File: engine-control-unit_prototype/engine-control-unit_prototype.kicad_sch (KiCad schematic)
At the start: 164 parts, among them J1 PORT_G, J2 PORT_E, J3 PORT_F, J4 PORT_A, J5 PORT_B, J6 PORT_D, J7 PORT_C, SW1 BOOT, U1 STM32H747II, Y1 32.768KHz, Y2 25MHz

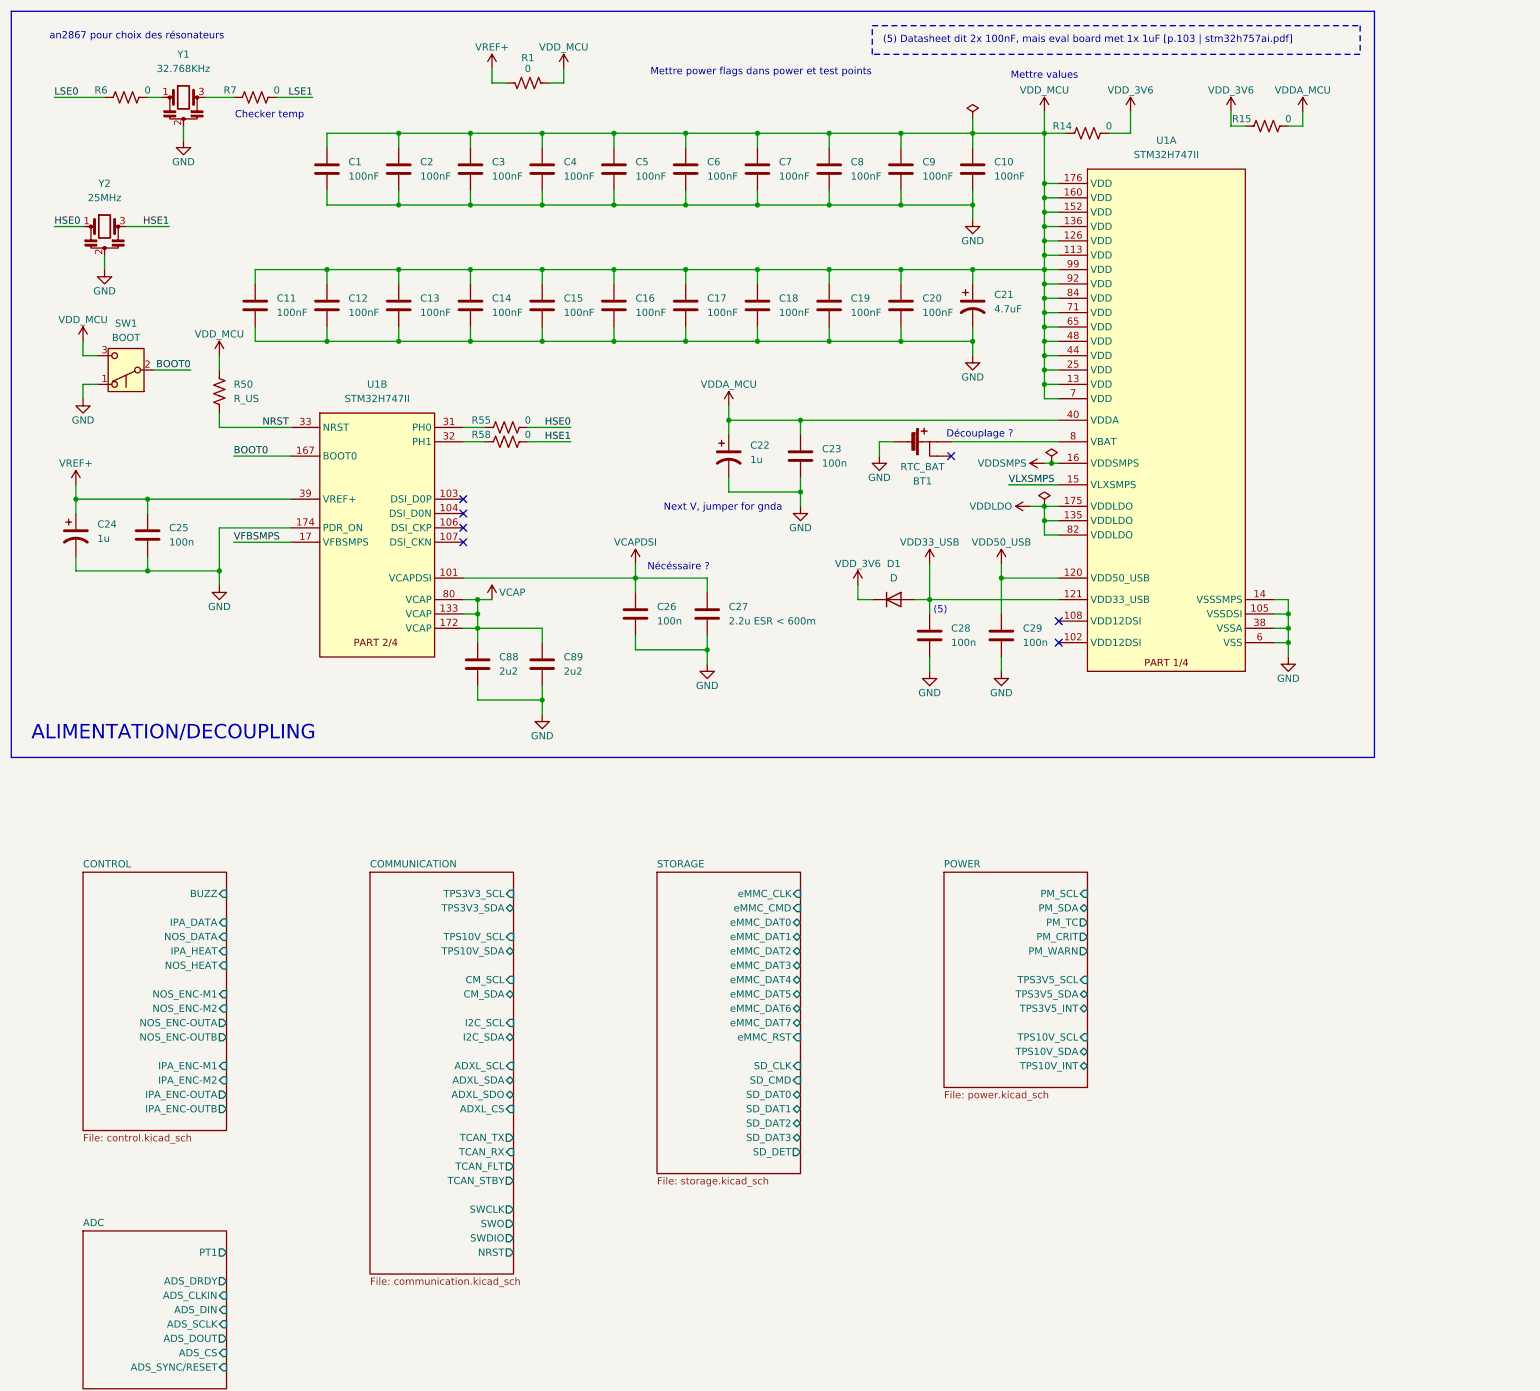
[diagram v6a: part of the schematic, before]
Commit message: Started layout Added some footprints
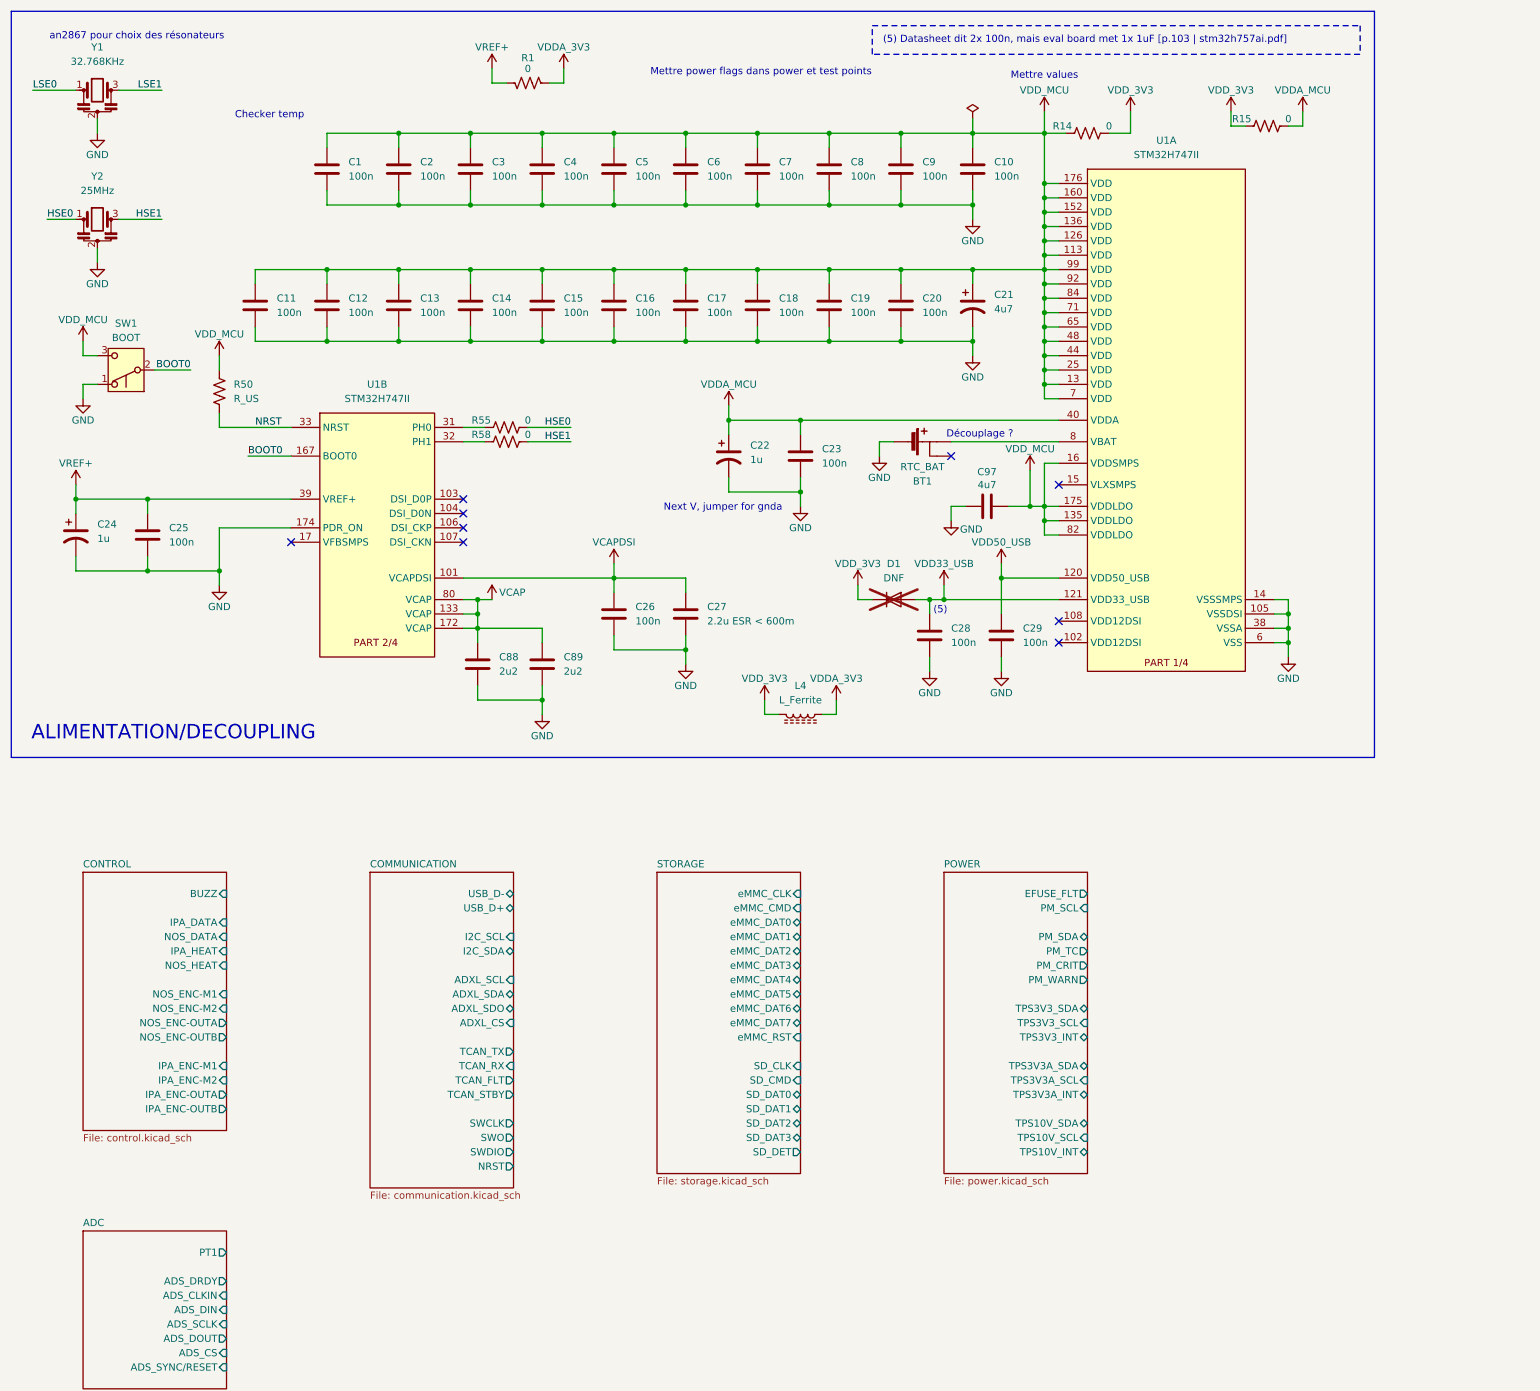
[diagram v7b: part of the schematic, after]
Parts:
- removed R6, R7: 0, Resistor_SMD:R_0201_0603Metric, symbol Device:R_US
- added C97: 4u7, Capacitor_SMD:C_0603_1608Metric, symbol Device:C
- added L4: L_Ferrite, Inductor_SMD:L_0603_1608Metric, symbol Device:L_Ferrite
- C1, C10, C11, C12, C13, C14, C15, C16, C17, C18, C19, C2, C20, C3, C4, C5, C6, C7, C8, C9: value 100nF -> 100n; footprint Capacitor_SMD:C_0603_1608Metric -> Capacitor_SMD:C_0402_1005Metric
- C21: value 4.7uF -> 4u7
- C23, C25, C26, C28, C29: footprint Capacitor_SMD:C_0603_1608Metric -> Capacitor_SMD:C_0402_1005Metric
- C27: footprint (none) -> Capacitor_SMD:C_0603_1608Metric
- D1: value D -> DNF; now not fitted
- J1, J2, J3, J4, J5, J6, J7: footprint (none) -> Connector_PinSocket_2.54mm:PinSocket_1x16_P2.54mm_Vertical
- SW1: footprint (none) -> Connector_PinSocket_2.54mm:PinSocket_1x03_P2.54mm_Vertical
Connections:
- net VDDLDO is gone; now on net VDD_MCU: U1.135 (VDDLDO), U1.175 (VDDLDO), U1.82 (VDDLDO)
- net VDDSMPS is gone; now on net VDD_MCU: U1.16 (VDDSMPS)
- net GND: now also C97.1
- net LSE0: now also Y1.1
- net LSE1: now also Y1.3
- net VDD_MCU: now also C97.2; no longer R1.1
- net VDD_3V6 renamed VDD_3V3
- net VDD_3V3: now also L4.2
- net VFBSMPS: no longer names the net of U1.17 (VFBSMPS)
- net VLXSMPS: no longer names the net of U1.15 (VLXSMPS)
- new net VDDA_3V3: L4.1, R1.1
- no-connect marks 7 -> 9
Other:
- sheet COMMUNICATION ports: added USB_D+, USB_D-; removed CM_SCL, CM_SDA, TPS10V_SCL, TPS10V_SDA, TPS3V3_SCL, TPS3V3_SDA
- sheet POWER ports: added EFUSE_FLT, TPS3V3A_INT, TPS3V3A_SCL, TPS3V3A_SDA, TPS3V3_INT, TPS3V3_SCL, TPS3V3_SDA; removed TPS3V5_INT, TPS3V5_SCL, TPS3V5_SDA
- note added: "(5) Datasheet dit 2x 100n, mais eval board met 1x 1uF [p.103 | stm32h757ai.pdf]"
- note removed: "(5) Datasheet dit 2x 100nF, mais eval board met 1x 1uF [p.103 | stm32h757ai.pdf]"
- note removed: "Nécéssaire ?"
- moved on the sheet: C26, C27, Y1, Y2

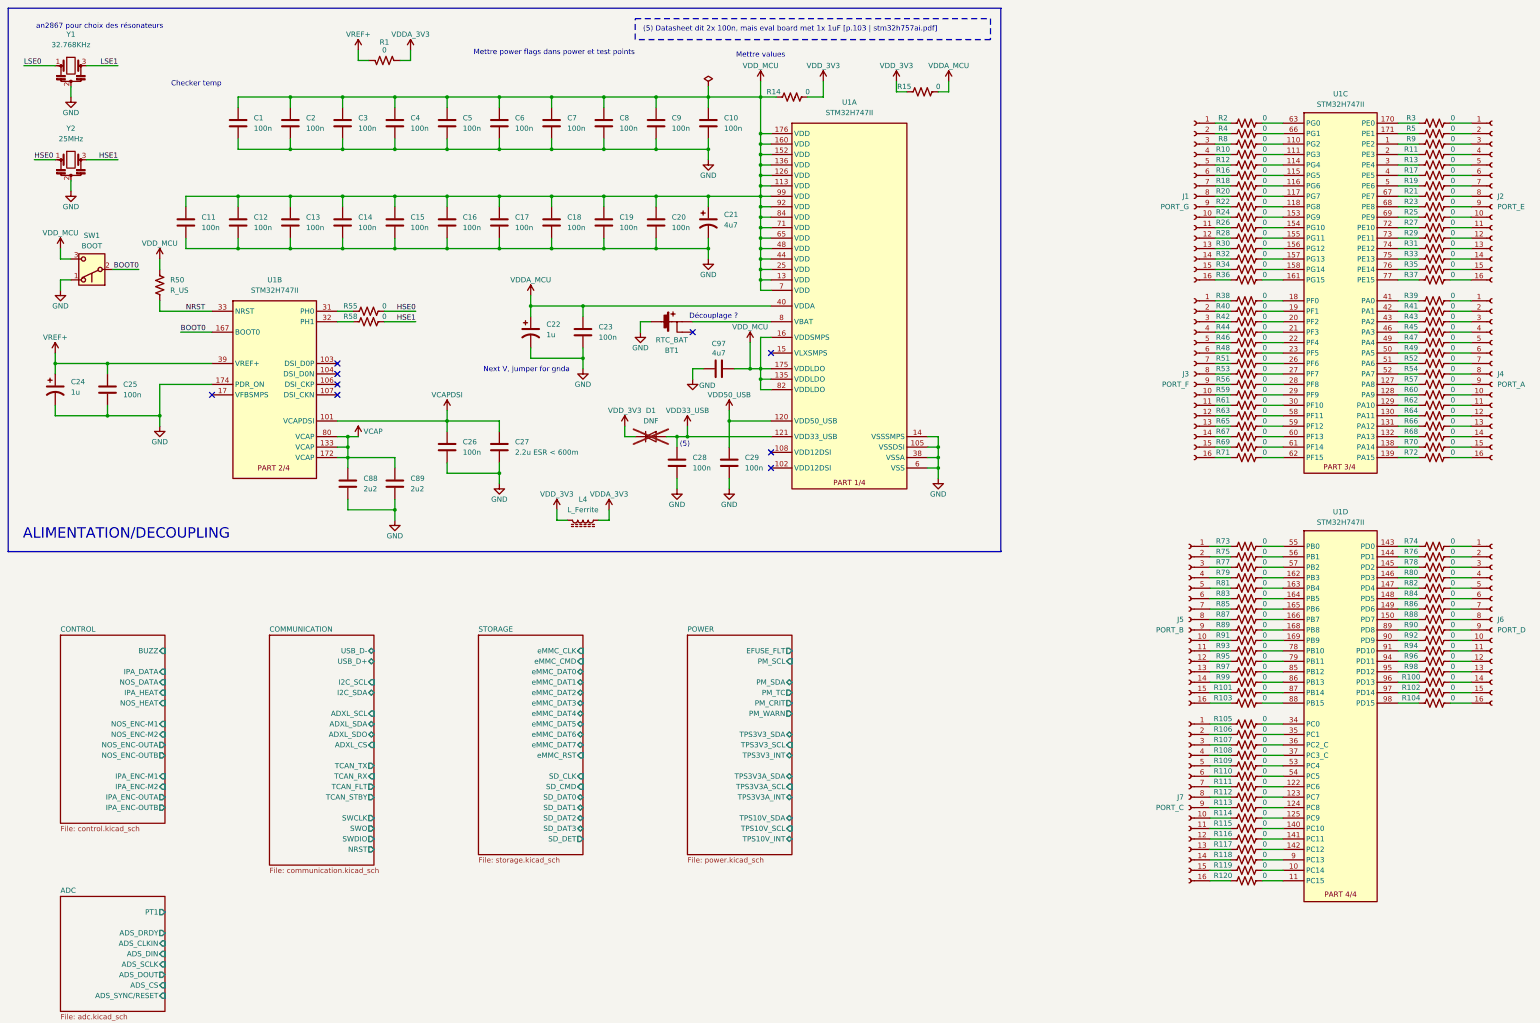
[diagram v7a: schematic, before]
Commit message: Added better LIB tree Continued PCB layout Some fixes Added chip for protection
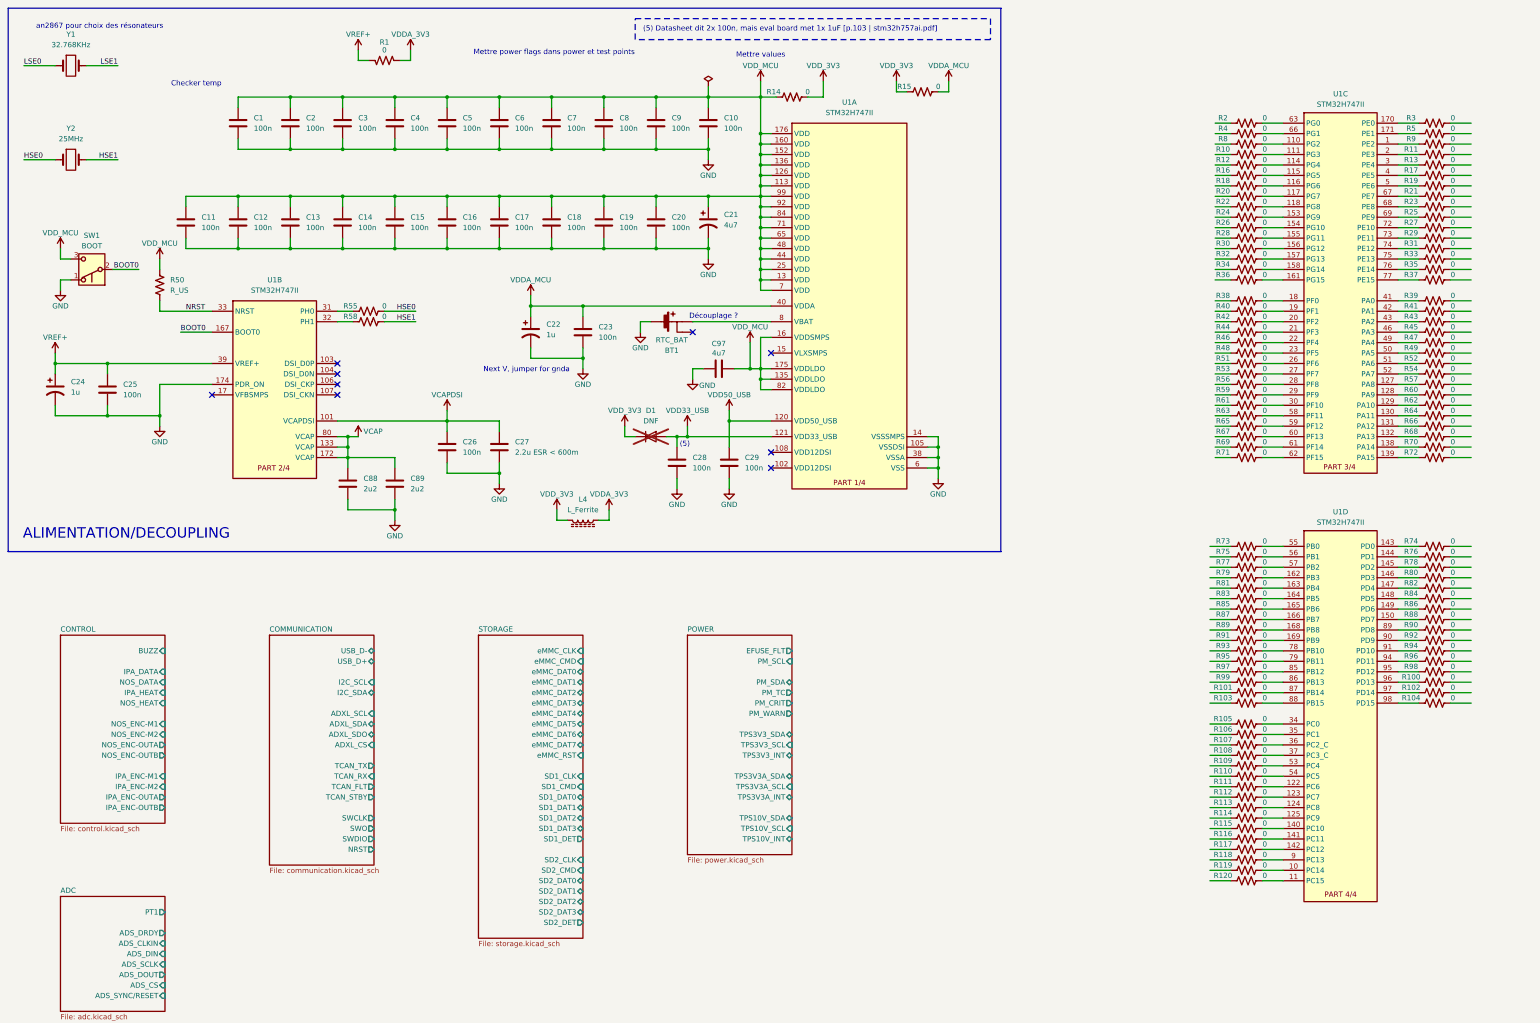
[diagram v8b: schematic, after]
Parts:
- removed J1: PORT_G, Connector_PinSocket_2.54mm:PinSocket_1x16_P2.54mm_Vertical, symbol Connector:Conn_01x16_Socket
- removed J2: PORT_E, Connector_PinSocket_2.54mm:PinSocket_1x16_P2.54mm_Vertical, symbol Connector:Conn_01x16_Socket
- removed J3: PORT_F, Connector_PinSocket_2.54mm:PinSocket_1x16_P2.54mm_Vertical, symbol Connector:Conn_01x16_Socket
- removed J4: PORT_A, Connector_PinSocket_2.54mm:PinSocket_1x16_P2.54mm_Vertical, symbol Connector:Conn_01x16_Socket
- removed J5: PORT_B, Connector_PinSocket_2.54mm:PinSocket_1x16_P2.54mm_Vertical, symbol Connector:Conn_01x16_Socket
- removed J6: PORT_D, Connector_PinSocket_2.54mm:PinSocket_1x16_P2.54mm_Vertical, symbol Connector:Conn_01x16_Socket
- removed J7: PORT_C, Connector_PinSocket_2.54mm:PinSocket_1x16_P2.54mm_Vertical, symbol Connector:Conn_01x16_Socket
- removed Y1: 32.768KHz, symbol Device:Resonator
- removed Y2: 25MHz, symbol Device:Resonator
- added Y1: 32.768KHz, symbol Device:Crystal
- added Y2: 25MHz, symbol Device:Crystal
- BT1: footprint 0CSL_D1_V1:BatteryHolder_BHX1_1025 -> Battery:Battery_Panasonic_CR2032-HFN_Horizontal_CircularHoles
- C21: footprint (none) -> Capacitor_SMD:CP_Elec_5x4.5
- SW1: footprint Connector_PinSocket_2.54mm:PinSocket_1x03_P2.54mm_Vertical -> Connector_PinSocket_1.27mm:PinSocket_1x03_P1.27mm_Vertical
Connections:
- net HSE0: now also Y2.1
- net HSE1: now also Y2.2
- net LSE0: now also Y1.1
- net LSE1: now also Y1.2
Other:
- sheet STORAGE ports: added SD1_CLK, SD1_CMD, SD1_DAT0, SD1_DAT1, SD1_DAT2, SD1_DAT3, SD1_DET, SD2_CLK, SD2_CMD, SD2_DAT0, SD2_DAT1, SD2_DAT2, SD2_DAT3, SD2_DET; removed SD_CLK, SD_CMD, SD_DAT0, SD_DAT1, SD_DAT2, SD_DAT3, SD_DET
